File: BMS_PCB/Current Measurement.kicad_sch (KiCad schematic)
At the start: 8 parts, among them U8 TLV2401

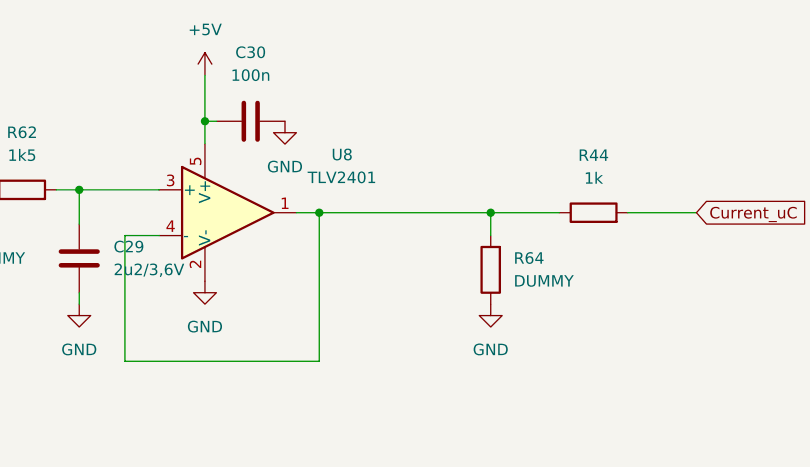
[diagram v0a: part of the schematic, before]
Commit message: Changes Schematic
- Symbol Relais
- add DUMMY
- changed Fuses 100mA
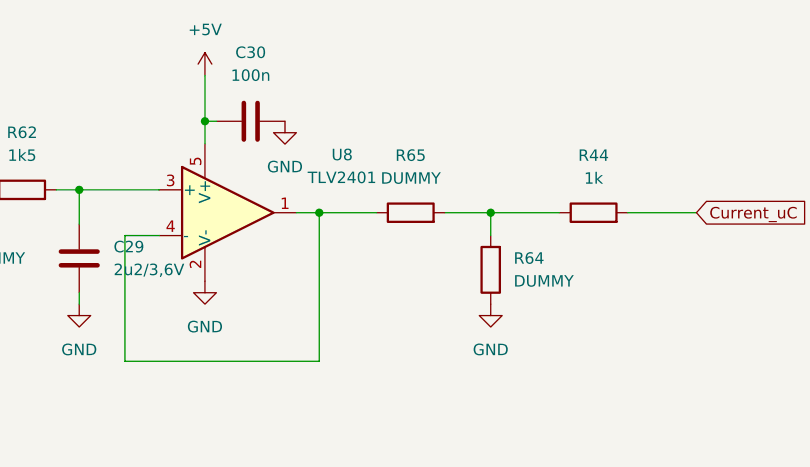
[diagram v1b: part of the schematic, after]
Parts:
- added R65: DUMMY, Resistor_SMD:R_0603_1608Metric_Pad0.98x0.95mm_HandSolder, symbol Device:R
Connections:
- net at U8.1, U8.4 (-): now also R65.1; no longer R44.1, R64.2
- new net: R44.1, R64.2, R65.2
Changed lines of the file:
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@@
 	(wire
 		(pts
-			(xy 88.9 49.53) (xy 107.95 49.53)
+			(xy 88.9 49.53) (xy 95.25 49.53)
 		)
 		(stroke
@@
 	(wire
 		(pts
-			(xy 46.99 46.99) (xy 52.07 46.99)
+			(xy 102.87 49.53) (xy 107.95 49.53)
 		)
 		(stroke
@@
 	(wire
 		(pts
-			(xy 71.12 52.07) (xy 67.31 52.07)
+			(xy 46.99 46.99) (xy 52.07 46.99)
 		)
 		(stroke
@@
 	(wire
 		(pts
-			(xy 88.9 49.53) (xy 88.9 66.04)
+			(xy 71.12 52.07) (xy 67.31 52.07)
 		)
 		(stroke
@@
 	(wire
 		(pts
-			(xy 76.2 39.37) (xy 77.47 39.37)
+			(xy 88.9 49.53) (xy 88.9 66.04)
 		)
 		(stroke
@@
 	(wire
 		(pts
-			(xy 107.95 49.53) (xy 115.57 49.53)
+			(xy 76.2 39.37) (xy 77.47 39.37)
 		)
 		(stroke
@@
 	(wire
 		(pts
-			(xy 86.36 49.53) (xy 88.9 49.53)
+			(xy 107.95 49.53) (xy 115.57 49.53)
 		)
 		(stroke
@@
 	(wire
 		(pts
-			(xy 76.2 34.29) (xy 76.2 39.37)
+			(xy 86.36 49.53) (xy 88.9 49.53)
 		)
 		(stroke
@@
 	(wire
 		(pts
-			(xy 67.31 66.04) (xy 88.9 66.04)
+			(xy 76.2 34.29) (xy 76.2 39.37)
 		)
 		(stroke
@@
 	(wire
 		(pts
-			(xy 123.19 49.53) (xy 130.81 49.53)
+			(xy 67.31 66.04) (xy 88.9 66.04)
 		)
 		(stroke
@@
 	(wire
 		(pts
-			(xy 107.95 49.53) (xy 107.95 52.07)
+			(xy 123.19 49.53) (xy 130.81 49.53)
 		)
 		(stroke
@@
 		)
 	)
+	(wire
+		(pts
+			(xy 107.95 49.53) (xy 107.95 52.07)
+		)
+		(stroke
+			(width 0)
+			(type default)
+		)
+	)
 	(global_label "Vcc_Current"
 		(shape output)
@@
 					(unit 1)
 				)
+			)
+		)
+	)
+	(symbol
+		(lib_id "Device:R")
+		(at 99.06 49.53 90)
+		(unit 1)
+		(exclude_from_sim no)
+		(in_bom yes)
+		(on_board yes)
+		(dnp no)
+		(fields_autoplaced yes)
+		(property "Reference" "R65"
+			(at 99.06 43.18 90)
+			(effects
+				(font
+					(size 1.27 1.27)
+				)
+			)
+		)
+		(property "Value" "DUMMY"
+			(at 99.06 45.72 90)
+			(effects
+				(font
+					(size 1.27 1.27)
+				)
+			)
+		)
+		(property "Footprint" "Resistor_SMD:R_0603_1608Metric_Pad0.98x0.95mm_HandSolder"
+			(at 99.06 51.308 90)
+			(effects
+				(font
+					(size 1.27 1.27)
+				)
+				(hide yes)
+			)
+		)
+		(property "Datasheet" "~"
+			(at 99.06 49.53 0)
+			(effects
+				(font
+					(size 1.27 1.27)
+				)
+				(hide yes)
+			)
+		)
+		(property "Description" "Resistor"
+			(at 99.06 49.53 0)
+			(effects
+				(font
+					(size 1.27 1.27)
+				)
+				(hide yes)
+			)
+		)
+		(pin "1"
+		)
+		(pin "2"
+		)
+		(instances
+			(project ""
+				(path "/f3f5bf67-59a2-4fff-a256-b414fb7b1786/97cd556a-bb13-4bbd-9a52-b5c25c14caba"
+					(reference "R65")
+					(unit 1)
+				)

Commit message: Footprints changes
-U10
-uC pins/SPI changes
- Fuses
- DSUB
- reupload layout
- etc.
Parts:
- R44: value 1k -> 100
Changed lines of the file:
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@@
 			)
 		)
-		(property "Value" "1k"
+		(property "Value" "100"
 			(at 119.38 45.72 90)
 			(effects

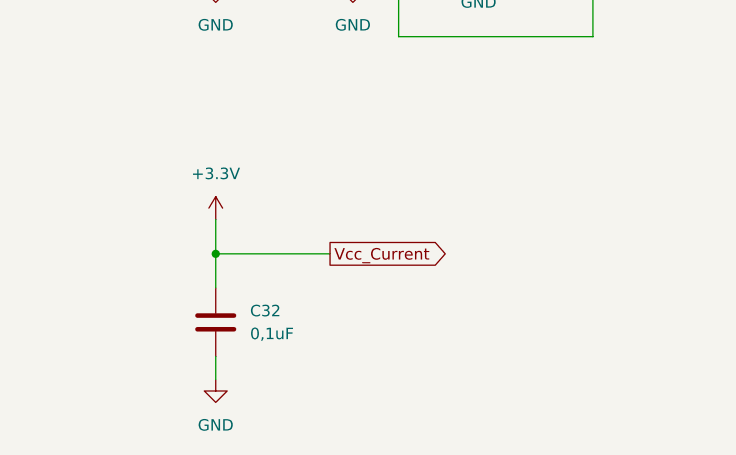
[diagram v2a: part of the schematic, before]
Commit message: changes schematic
still missing: uC pins
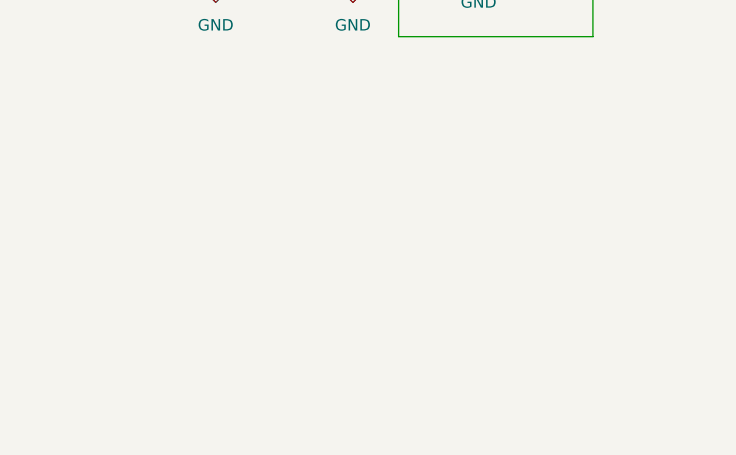
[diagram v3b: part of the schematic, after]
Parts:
- removed C32: 0,1uF, Capacitor_SMD:C_0603_1608Metric_Pad1.08x0.95mm_HandSolder, symbol Device:C
